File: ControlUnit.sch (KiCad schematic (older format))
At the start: 55 parts, among them SW1 SW_Push-Switch, U22 7400, U23 74LS161-74xx, U24 AT28C256, U25 AT28C256, U38 74LS138, U42 74LS138, U43 74LS138

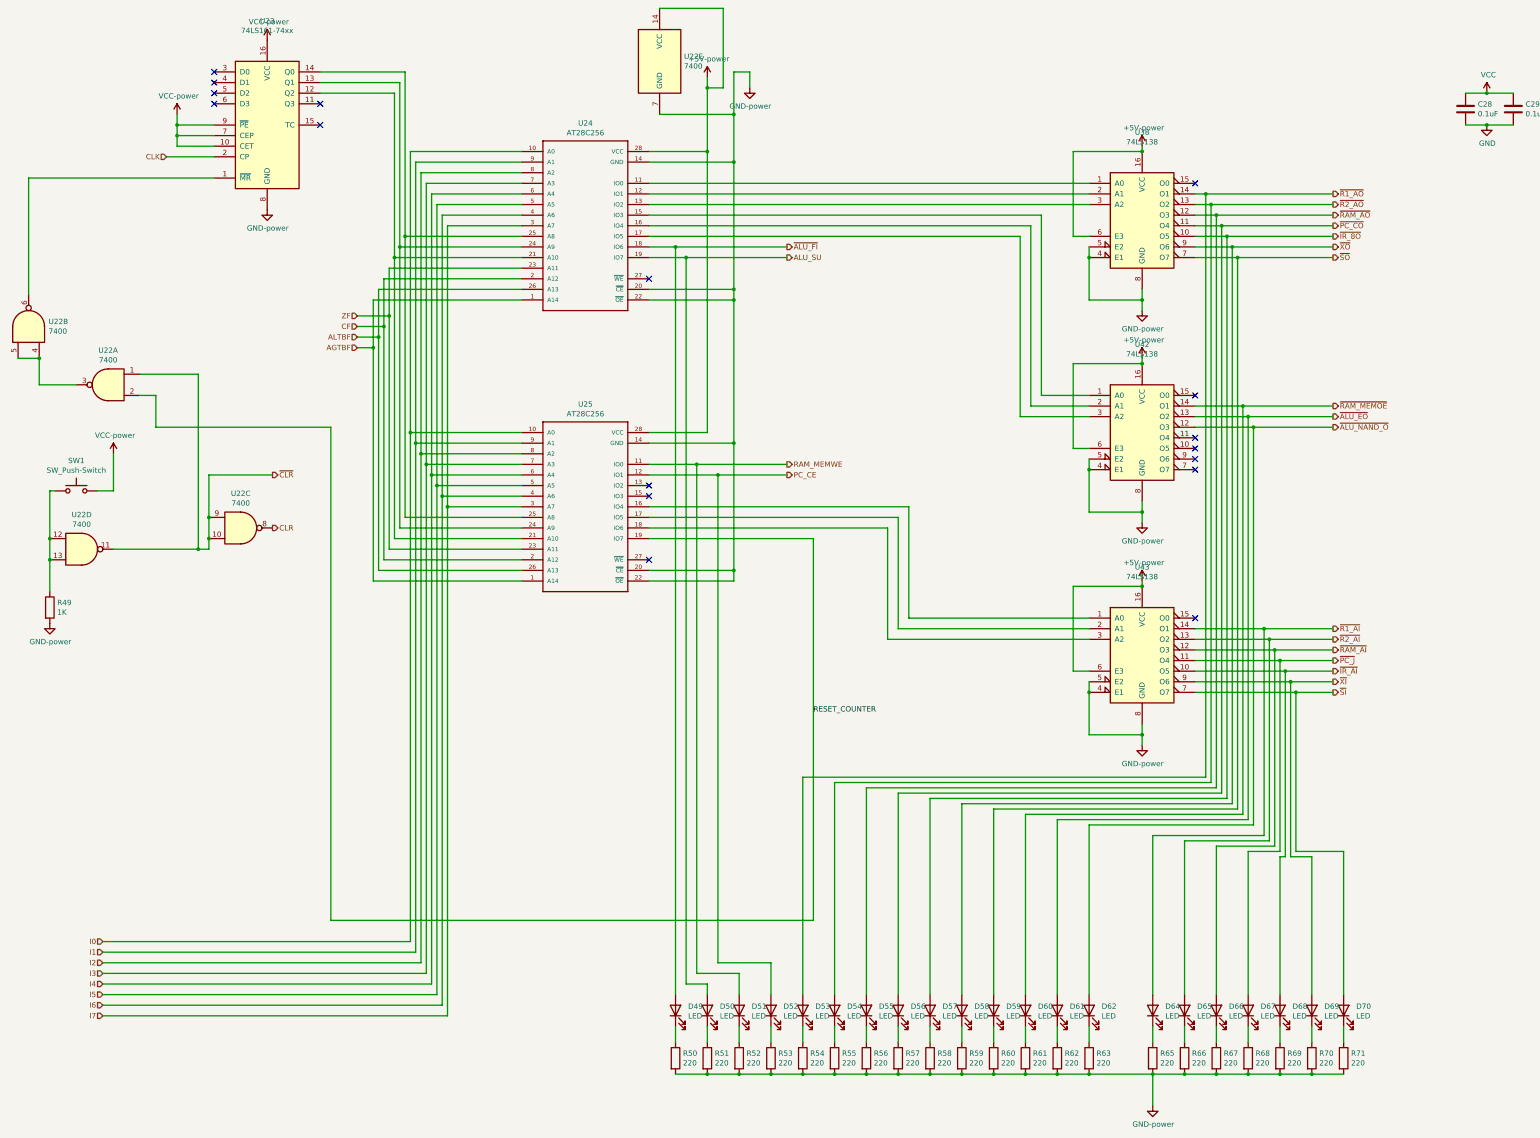
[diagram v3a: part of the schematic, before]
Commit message: added display
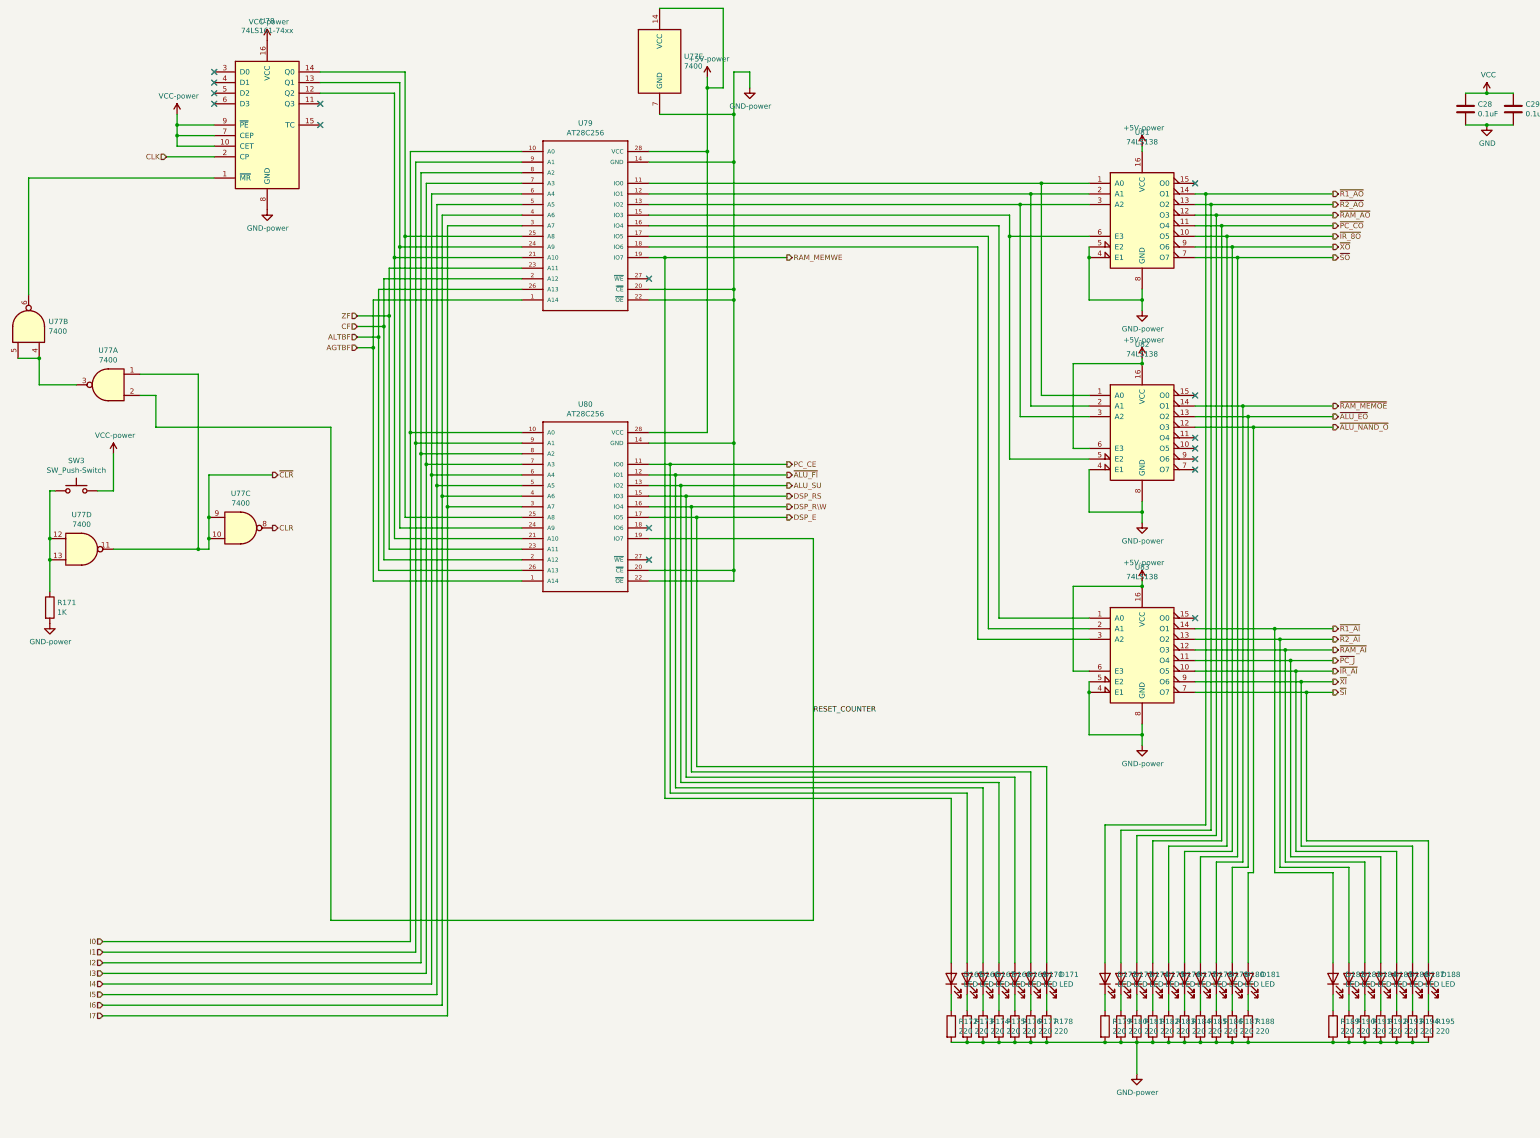
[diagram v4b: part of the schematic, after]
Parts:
- removed D49, D50, D51, D52, D53, D54, D55, D56, D57, D58, D59, D60, D61, D62, D64, D65, D66, D67, D68: LED, LED_THT:LED_D3.0mm, symbol Device:LED
- removed R50, R51, R52, R53, R54, R55, R56, R57, R58, R59, R60, R61, R62, R63, R65, R66, R67, R68, R69: 220, Resistor_THT:R_Axial_DIN0204_L3.6mm_D1.6mm_P7.62mm_Horizontal, symbol Device:R
- added D165, D166, D167, D168, D169, D170, D171, D172, D173, D174, D175, D176, D177, D178, D179, D180, D181, D182, D183, D184, D185, D186: LED, LED_THT:LED_D3.0mm, symbol Device:LED
- added R172, R173, R174, R175, R176, R177, R178, R179, R180, R181, R182, R183, R184, R185, R186, R187, R188, R189, R190, R191, R192, R193: 220, Resistor_THT:R_Axial_DIN0204_L3.6mm_D1.6mm_P7.62mm_Horizontal, symbol Device:R
- renumbered D69 to D187, D70 to D188, R49 to R171, R70 to R194, R71 to R195, SW1 to SW3, U22 to U77, U23 to U78, U24 to U79, U25 to U80, U38 to U81, U42 to U82, U43 to U83
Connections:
- net +5V: no longer U81.6 (E3)
- net ALU_SU: now also U80.13 (IO2), D168.2 (A); no longer U79.19 (IO7)
- net GND: now also R172.2, R173.2, R174.2, R175.2, R176.2, R177.2, R178.2, R179.2, R180.2, R181.2, R182.2, R183.2, R184.2, R185.2, R186.2, R187.2, R188.2, R189.2, R190.2, R191.2, R192.2, R193.2; no longer U82.5 (E2)
- net PC_CE: now also U80.11 (IO0), D166.2 (A); no longer U80.12 (IO1)
- net RAM_MEMWE: now also U79.19 (IO7), D165.2 (A); no longer U80.11 (IO0)
- net ~ALU_EO: now also D180.2 (A)
- net ~ALU_FI: now also U80.12 (IO1), D167.2 (A); no longer U79.18 (IO6)
- net ~ALU_NAND_O: now also D181.2 (A)
- net ~IR_8O: now also D176.2 (A)
- net ~IR_AI: now also D186.2 (A)
- net ~PC_CO: now also D175.2 (A)
- net ~PC_J: now also D185.2 (A)
- net ~R1_AI: now also D182.2 (A)
- net ~R1_AO: now also D172.2 (A)
- net ~R2_AI: now also D183.2 (A)
- net ~R2_AO: now also D173.2 (A)
- net ~RAM_AI: now also D184.2 (A)
- net ~RAM_AO: now also D174.2 (A)
- net ~RAM_MEMOE: now also D179.2 (A)
- net ~SO: now also D178.2 (A)
- net ~XO: now also D177.2 (A)
- net at U79.11 (IO0), U81.1 (A0): now also U82.1 (A0)
- net at U79.12 (IO1), U81.2 (A1): now also U82.2 (A1)
- net at U79.13 (IO2), U81.3 (A2): now also U82.3 (A2)
- net at U79.15 (IO3): now also U81.6 (E3), U82.5 (E2); no longer U82.1 (A0)
- net at U79.16 (IO4): now also U83.1 (A0); no longer U82.2 (A1)
- net at U79.17 (IO5): now also U83.2 (A1); no longer U82.3 (A2)
- net DSP_RS: now reaches U80.15 (IO3)
- net DSP_RS: now also D169.2 (A)
- net DSP_R\W: now reaches U80.16 (IO4)
- net DSP_R\W: now also D170.2 (A); no longer U83.1 (A0)
- net DSP_E: now reaches U80.17 (IO5)
- net DSP_E: now also D171.2 (A); no longer U83.2 (A1)
- net at U83.3 (A2): now also U79.18 (IO6); no longer U80.18 (IO6)
- new net: D186.1 (K), R193.1
- new net: D185.1 (K), R192.1
- new net: D184.1 (K), R191.1
- new net: D183.1 (K), R190.1
- new net: D182.1 (K), R189.1
- new net: D181.1 (K), R188.1
- new net: D180.1 (K), R187.1
- new net: D179.1 (K), R186.1
- new net: D178.1 (K), R185.1
- new net: D177.1 (K), R184.1
- new net: D176.1 (K), R183.1
- new net: D175.1 (K), R182.1
- new net: D174.1 (K), R181.1
- new net: D173.1 (K), R180.1
- new net: D172.1 (K), R179.1
- new net: D171.1 (K), R178.1
- new net: D170.1 (K), R177.1
- new net: D169.1 (K), R176.1
- new net: D168.1 (K), R175.1
- new net: D167.1 (K), R174.1
- new net: D166.1 (K), R173.1
- new net: D165.1 (K), R172.1
- no-connect marks 17 -> 16
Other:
- moved on the sheet: D187, D188, R194, R195

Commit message: added display
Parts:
- added D189: LED, LED_THT:LED_D3.0mm, symbol Device:LED
- added R196: 220, Resistor_THT:R_Axial_DIN0204_L3.6mm_D1.6mm_P7.62mm_Horizontal, symbol Device:R
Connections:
- net GND: now also R196.2
- net RESET_COUNTER: now also D189.2 (A)
- new net: D189.1 (K), R196.1
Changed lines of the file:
@@
 Wire Wire Line
 	13350 7400 13600 7400
+$Comp
+L Device:R R?
+U 1 1 61158337
+P 8700 10550
+AR Path="/5F926C74/61158337" Ref="R?"  Part="1"
+AR Path="/61968B9B/60C9B37A/61158337" Ref="R?"  Part="1"
+AR Path="/5F67C726/60E31E38/61158337" Ref="R?"  Part="1"
+AR Path="/5F74778C/60E31E38/61158337" Ref="R?"  Part="1"
+AR Path="/5F5F4A69/61054F55/61158337" Ref="R?"  Part="1"
+AR Path="/5F6ACD14/6156E9B6/61158337" Ref="R?"  Part="1"
+AR Path="/5F681977/6183038C/61158337" Ref="R?"  Part="1"
+AR Path="/5F681977/61B5B13E/61158337" Ref="R?"  Part="1"
+AR Path="/5F79B702/621E2556/61158337" Ref="R?"  Part="1"
+AR Path="/61DF6CC7/623AC6EB/61158337" Ref="R?"  Part="1"
+AR Path="/5FD099BF/625B6FDA/61158337" Ref="R?"  Part="1"
+AR Path="/5FD099BF/61158337" Ref="R196"  Part="1"
+F 0 "R196" H 8770 10596 50  0000 L CNN
+F 1 "220" H 8770 10505 50  0000 L CNN
+F 2 "Resistor_THT:R_Axial_DIN0204_L3.6mm_D1.6mm_P7.62mm_Horizontal" V 8630 10550 50  0001 C CNN
+F 3 "" H 8700 10550 50  0001 C CNN
+	1    8700 10550
+	1    0    0    -1
+$EndComp
+Wire Wire Line
+	8700 10250 8700 10400
+$Comp
+L Device:LED D?
+U 1 1 6115833E
+P 8700 10100
+AR Path="/5F926C74/6115833E" Ref="D?"  Part="1"
+AR Path="/61968B9B/60C9B37A/6115833E" Ref="D?"  Part="1"
+AR Path="/5F67C726/60E31E38/6115833E" Ref="D?"  Part="1"
+AR Path="/5F74778C/60E31E38/6115833E" Ref="D?"  Part="1"
+AR Path="/5F5F4A69/61054F55/6115833E" Ref="D?"  Part="1"
+AR Path="/5F6ACD14/6156E9B6/6115833E" Ref="D?"  Part="1"
+AR Path="/5F681977/6183038C/6115833E" Ref="D?"  Part="1"
+AR Path="/5F681977/61B5B13E/6115833E" Ref="D?"  Part="1"
+AR Path="/5F79B702/621E2556/6115833E" Ref="D?"  Part="1"
+AR Path="/61DF6CC7/623AC6EB/6115833E" Ref="D?"  Part="1"
+AR Path="/5FD099BF/625B6FDA/6115833E" Ref="D?"  Part="1"
+AR Path="/5FD099BF/6115833E" Ref="D189"  Part="1"
+F 0 "D189" V 8739 9982 50  0000 R CNN
+F 1 "LED" V 8648 9982 50  0000 R CNN
+F 2 "LED_THT:LED_D3.0mm" H 8700 10100 50  0001 C CNN
+F 3 "" H 8700 10100 50  0001 C CNN
+	1    8700 10100
+	0    -1   -1   0
+$EndComp
+Wire Wire Line
+	8700 9950 8700 9550
+Connection ~ 8700 9550
+Wire Wire Line
+	8700 10700 8700 11000
+$Comp
+L 16bitCpu-rescue:GND-power #PWR?
+U 1 1 611D35A4
+P 8700 11000
+AR Path="/5F926C74/611D35A4" Ref="#PWR?"  Part="1"
+AR Path="/61968B9B/60C9B37A/611D35A4" Ref="#PWR?"  Part="1"
+AR Path="/5F67C726/60E31E38/611D35A4" Ref="#PWR?"  Part="1"
+AR Path="/5F74778C/60E31E38/611D35A4" Ref="#PWR?"  Part="1"
+AR Path="/5F5F4A69/61054F55/611D35A4" Ref="#PWR?"  Part="1"
+AR Path="/5F6ACD14/6156E9B6/611D35A4" Ref="#PWR?"  Part="1"
+AR Path="/5F681977/6183038C/611D35A4" Ref="#PWR?"  Part="1"
+AR Path="/5F681977/61B5B13E/611D35A4" Ref="#PWR?"  Part="1"
+AR Path="/5F79B702/621E2556/611D35A4" Ref="#PWR?"  Part="1"
+AR Path="/61DF6CC7/623AC6EB/611D35A4" Ref="#PWR?"  Part="1"
+AR Path="/5FD099BF/625B6FDA/611D35A4" Ref="#PWR?"  Part="1"
+AR Path="/5FD099BF/611D35A4" Ref="#PWR0268"  Part="1"
+F 0 "#PWR0268" H 8700 10750 50  0001 C CNN
+F 1 "GND-power" H 8705 10827 50  0000 C CNN
+F 2 "" H 8700 11000 50  0001 C CNN
+F 3 "" H 8700 11000 50  0001 C CNN
+	1    8700 11000
+	1    0    0    -1
+$EndComp
 $EndSCHEMATC

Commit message: added swp_x, and cleanup readme
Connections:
- net I0: now also U79.7 (A3), U80.7 (A3); no longer U79.10 (A0), U80.10 (A0)
- net I1: now also U79.6 (A4), U80.6 (A4); no longer U79.9 (A1), U80.9 (A1)
- net I2: now also U79.5 (A5), U80.5 (A5); no longer U79.8 (A2), U80.8 (A2)
- net I3: now also U79.4 (A6), U80.4 (A6); no longer U79.7 (A3), U80.7 (A3)
- net I4: now also U79.3 (A7), U80.3 (A7); no longer U79.6 (A4), U80.6 (A4)
- net I5: now also U79.25 (A8), U80.25 (A8); no longer U79.5 (A5), U80.5 (A5)
- net I6: now also U79.24 (A9), U80.24 (A9); no longer U79.4 (A6), U80.4 (A6)
- net I7: now also U79.21 (A10), U80.21 (A10); no longer U79.3 (A7), U80.3 (A7)
- net ~X_SWP_O: now reaches U82.11 (O4)
- net ~HLT: now reaches U82.7 (O7)
- new net: U78.12 (Q2), U79.10 (A0), U80.10 (A0)
- new net: U78.13 (Q1), U79.9 (A1), U80.9 (A1)
- new net: U78.14 (Q0), U79.8 (A2), U80.8 (A2)
- no-connect marks 16 -> 14
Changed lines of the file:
@@
 	7150 2400 7950 2400
 Connection ~ 7950 2400
-Wire Wire Line
-	4750 1750 4750 3300
-Wire Wire Line
-	4800 1650 4800 3200
-Wire Wire Line
-	4850 1550 4850 3100
-Wire Wire Line
-	4900 2300 5950 2300
-Wire Wire Line
-	4950 2400 5950 2400
-Wire Wire Line
-	5000 2500 5950 2500
-Wire Wire Line
-	5050 2600 5950 2600
-Wire Wire Line
-	5100 2700 5950 2700
-Wire Wire Line
-	5150 2800 5950 2800
-Wire Wire Line
-	5200 2900 5950 2900
-Wire Wire Line
-	5250 3000 5950 3000
-Wire Wire Line
-	4850 3100 5950 3100
-Connection ~ 4850 3100
-Wire Wire Line
-	4800 3200 5950 3200
-Connection ~ 4800 3200
-Wire Wire Line
-	4800 3200 4800 5850
-Wire Wire Line
-	4750 3300 5950 3300
-Connection ~ 4750 3300
-Wire Wire Line
-	4750 3300 4750 5950
-Wire Wire Line
-	4700 3400 5950 3400
-Wire Wire Line
-	4650 3500 5950 3500
 Text HLabel 4400 4050 0    50   Input ~ 0
 ALTBF
@@
 Wire Wire Line
 	4400 4050 4600 4050
-Wire Wire Line
-	4600 3600 5950 3600
 Connection ~ 4650 3950
 Connection ~ 4700 3850
@@
 Wire Wire Line
 	4550 4150 4550 3700
-Wire Wire Line
-	4550 3700 5950 3700
 $Comp
 L AT28C256:AT28C256 U80
@@
 $EndComp
 Wire Wire Line
-	5950 4950 4900 4950
-Wire Wire Line
-	4900 2300 4900 4950
-Connection ~ 4900 4950
-Wire Wire Line
-	4900 4950 4900 9750
-Wire Wire Line
-	5950 5050 4950 5050
-Wire Wire Line
-	4950 2400 4950 5050
-Connection ~ 4950 5050
-Wire Wire Line
-	4950 5050 4950 9850
-Wire Wire Line
-	5950 5150 5000 5150
-Wire Wire Line
-	5000 2500 5000 5150
-Connection ~ 5000 5150
-Wire Wire Line
-	5000 5150 5000 9950
-Wire Wire Line
-	5100 2700 5100 5350
-Wire Wire Line
-	5950 5250 5050 5250
-Wire Wire Line
-	5050 2600 5050 5250
-Connection ~ 5050 5250
-Wire Wire Line
-	5050 5250 5050 10050
-Wire Wire Line
-	5950 5350 5100 5350
-Connection ~ 5100 5350
-Wire Wire Line
-	5100 5350 5100 10150
-Wire Wire Line
-	5150 2800 5150 5450
-Connection ~ 5150 5450
-Wire Wire Line
-	5150 5450 5150 10250
-Wire Wire Line
-	5950 5550 5200 5550
-Connection ~ 5200 5550
-Wire Wire Line
-	5200 5550 5200 10350
-Wire Wire Line
-	5950 5650 5250 5650
-Wire Wire Line
-	5250 3000 5250 5650
-Connection ~ 5250 5650
-Wire Wire Line
-	5250 5650 5250 10450
-Wire Wire Line
-	5150 5450 5950 5450
-Wire Wire Line
-	5200 2900 5200 5550
-Wire Wire Line
-	5950 5750 4850 5750
-Wire Wire Line
-	4850 3100 4850 5750
-Wire Wire Line
-	5950 5850 4800 5850
-Wire Wire Line
-	5950 5950 4750 5950
-Wire Wire Line
-	5950 6050 4700 6050
-Wire Wire Line
 	4700 3850 4700 6050
 Wire Wire Line
-	4650 6150 5950 6150
-Wire Wire Line
 	4650 6150 4650 3950
-Wire Wire Line
-	5950 6250 4600 6250
 Wire Wire Line
 	4600 6250 4600 4050
 Connection ~ 4600 4050
-Wire Wire Line
-	4550 4150 4550 6350
-Wire Wire Line
-	4550 6350 5950 6350
 Connection ~ 4550 4150
 Wire Wire Line
@@
 	2500 4900 4150 4900
 NoConn ~ 12300 6700
-NoConn ~ 12300 5300
 NoConn ~ 12300 5200
 NoConn ~ 12300 5100
-NoConn ~ 12300 5000
 NoConn ~ 12300 4600
 NoConn ~ 4050 2050
@@
 	1    0    0    -1
 $EndComp
+Wire Wire Line
+	4850 1550 4850 2500
+Wire Wire Line
+	4800 1650 4800 2400
+Wire Wire Line
+	4900 2600 4900 5250
+Wire Wire Line
+	4950 2700 4950 5350
+Wire Wire Line
+	5000 2800 5000 5450
+Wire Wire Line
+	5050 2900 5050 5550
+Wire Wire Line
+	5100 3000 5100 5650
+Wire Wire Line
+	5950 3100 5150 3100
+Wire Wire Line
+	5150 3100 5150 5750
+Wire Wire Line
+	5950 3200 5200 3200
+Wire Wire Line
+	5200 3200 5200 5850
+Wire Wire Line
+	5950 3300 5250 3300
+Wire Wire Line
+	5250 3300 5250 5950
+Wire Wire Line
+	5100 3000 5950 3000
+Wire Wire Line
+	5050 2900 5950 2900
+Wire Wire Line
+	5000 2800 5950 2800
+Wire Wire Line
+	4950 2700 5950 2700
+Wire Wire Line
+	4900 2600 5950 2600
+Wire Wire Line
+	5950 2300 4750 2300
+Wire Wire Line
+	4750 1750 4750 2300
+Connection ~ 4750 2300
+Wire Wire Line
+	5950 2400 4800 2400
+Connection ~ 4800 2400
+Wire Wire Line
+	4800 2400 4800 5050
+Wire Wire Line
+	5950 2500 4850 2500
+Connection ~ 4850 2500
+Wire Wire Line
+	4850 2500 4850 5150
+Wire Wire Line
+	5950 3400 4700 3400
+Wire Wire Line
+	4650 3500 5950 3500
+Wire Wire Line
+	4600 3600 5950 3600
+Wire Wire Line
+	5950 3700 4550 3700
+Wire Wire Line
+	5950 4950 4750 4950
+Wire Wire Line
+	4750 2300 4750 4950
+Wire Wire Line
+	5950 5050 4800 5050
+Wire Wire Line
+	5950 5150 4850 5150
+Wire Wire Line
+	5950 5250 4900 5250
+Connection ~ 4900 5250
+Wire Wire Line
+	4900 5250 4900 9750
+Wire Wire Line
+	4950 5350 5950 5350
+Connection ~ 4950 5350
+Wire Wire Line
+	4950 5350 4950 9850
+Wire Wire Line
+	5000 5450 5950 5450
+Connection ~ 5000 5450
+Wire Wire Line
+	5000 5450 5000 9950
+Wire Wire Line
+	5050 5550 5950 5550
+Connection ~ 5050 5550
+Wire Wire Line
+	5050 5550 5050 10050
+Wire Wire Line
+	5100 5650 5950 5650
+Connection ~ 5100 5650
+Wire Wire Line
+	5100 5650 5100 10150
+Wire Wire Line
+	5150 5750 5950 5750
+Connection ~ 5150 5750
+Wire Wire Line
+	5150 5750 5150 10250
+Wire Wire Line
+	5200 5850 5950 5850
+Connection ~ 5200 5850
+Wire Wire Line
+	5200 5850 5200 10350
+Wire Wire Line
+	5250 5950 5950 5950
+Connection ~ 5250 5950
+Wire Wire Line
+	5250 5950 5250 10450
+Wire Wire Line
+	5950 6350 4550 6350
+Wire Wire Line
+	4550 4150 4550 6350
+Wire Wire Line
+	5950 6250 4600 6250
+Wire Wire Line
+	4650 6150 5950 6150
+Wire Wire Line
+	5950 6050 4700 6050
+Wire Wire Line
+	12300 5300 13600 5300
+Text HLabel 13600 5300 2    50   Output ~ 0
+~HLT
+Wire Wire Line
+	12300 5000 13600 5000
+Text HLabel 13600 5000 2    50   Output ~ 0
+~X_SWP_O
 $EndSCHEMATC

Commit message: clean up
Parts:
- renumbered D189 to D165, D165 to D166, D166 to D167, D167 to D168, D168 to D169, D169 to D170, D170 to D171, D171 to D172, D172 to D173, D173 to D174, D174 to D175, D175 to D176, D176 to D177, D177 to D178, D178 to D179, D179 to D180, D180 to D181, D181 to D182, D182 to D183, D183 to D184, D184 to D185, D185 to D186, D186 to D187, D187 to D188, D188 to D189, R196 to R172, R172 to R173, R173 to R174, R174 to R175, R175 to R176, R176 to R177, R177 to R178, R178 to R179, R179 to R180, R180 to R181, R181 to R182, R182 to R183, R183 to R184, R184 to R185, R185 to R186, R186 to R187, R187 to R188, R188 to R189, R189 to R190, R190 to R191, R191 to R192, R192 to R193, R193 to R194, R194 to R195, R195 to R196, U77 to U79, U78 to U80, U79 to U81, U80 to U82, U81 to U83, U82 to U84, U83 to U85
